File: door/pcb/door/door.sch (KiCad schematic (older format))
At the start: 0 parts

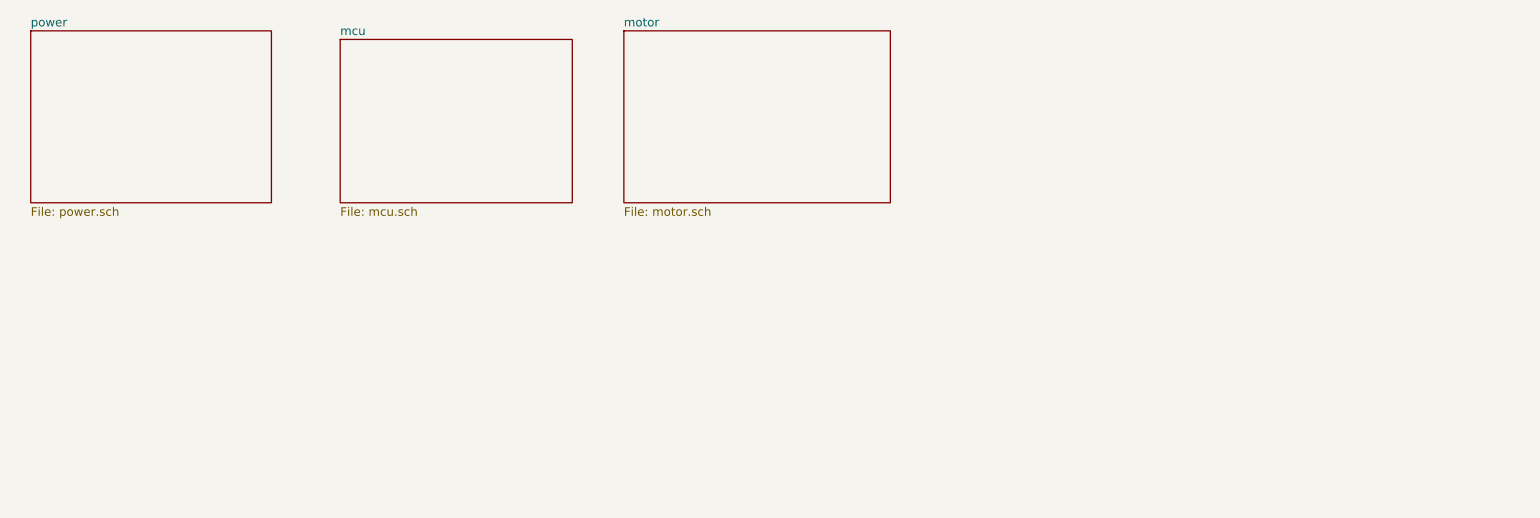
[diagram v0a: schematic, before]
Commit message: added silkscreen labels for the usart pin header
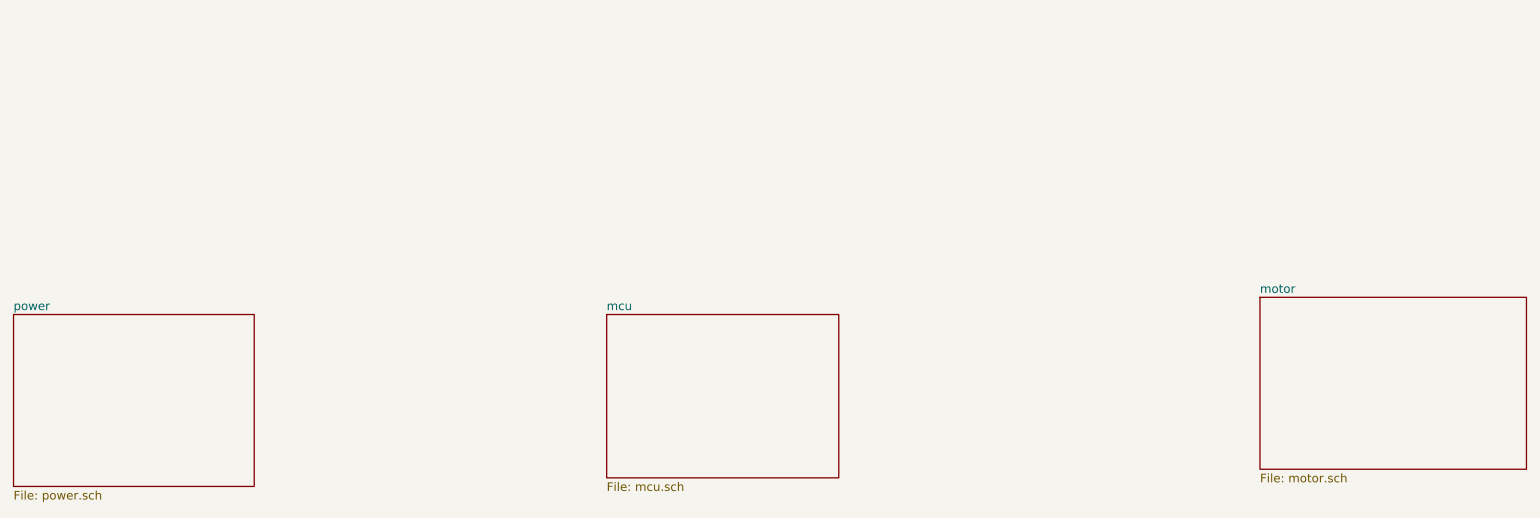
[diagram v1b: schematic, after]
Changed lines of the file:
@@
 $EndDescr
 $Sheet
-S 1750 1250 1400 1000
+S 1650 2900 1400 1000
 U 5BE80860
 F0 "power" 50
@@
 $EndSheet
 $Sheet
-S 3550 1300 1350 950
+S 5100 2900 1350 950
 U 5BE80873
 F0 "mcu" 50
@@
 $EndSheet
 $Sheet
-S 5200 1250 1550 1000
+S 8900 2800 1550 1000
 U 5BEA7097
 F0 "motor" 50
